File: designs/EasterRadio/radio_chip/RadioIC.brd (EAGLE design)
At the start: 38 x 29 mm, 26 parts, among them J1 S2B-NSHSS-TB, J2 S2B-NSHSS-TB, Q1 2SC3838T146, Y1 32.768kHz crystal

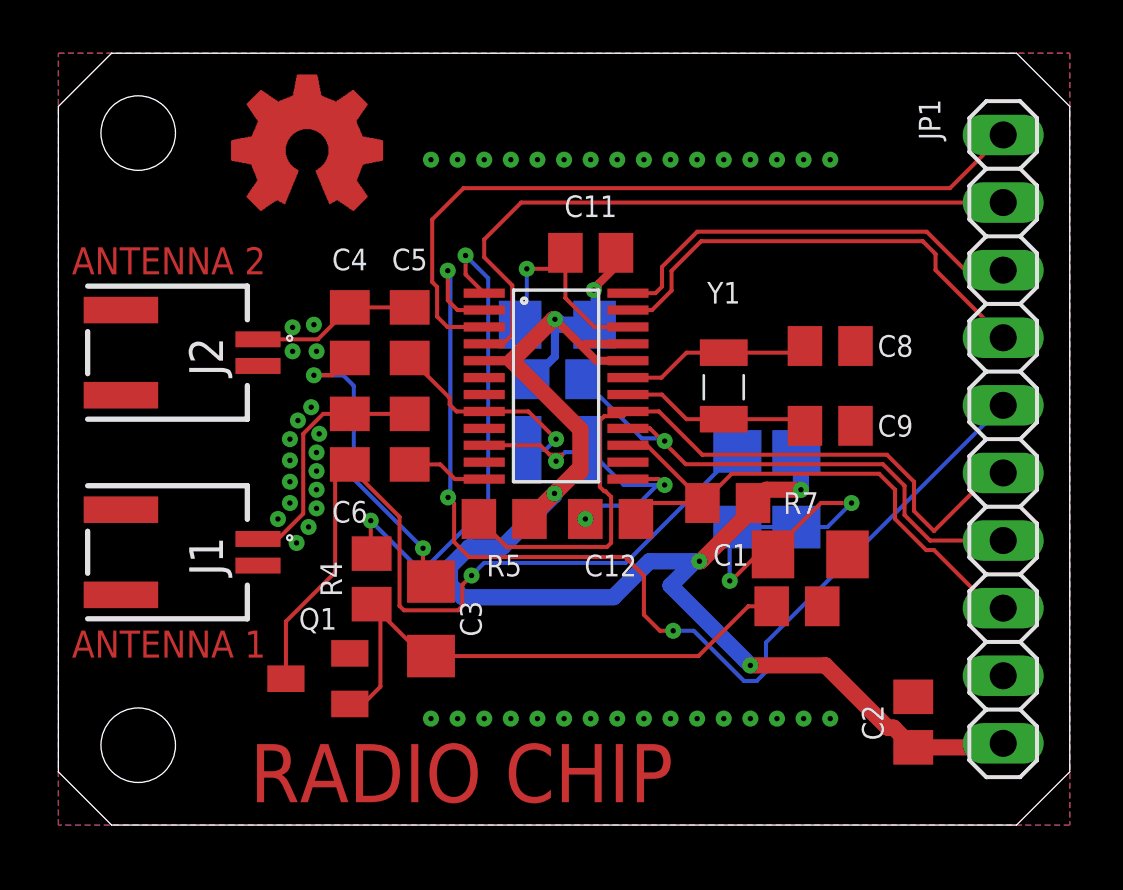
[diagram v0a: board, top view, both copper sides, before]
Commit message: added esd for rs232 to can
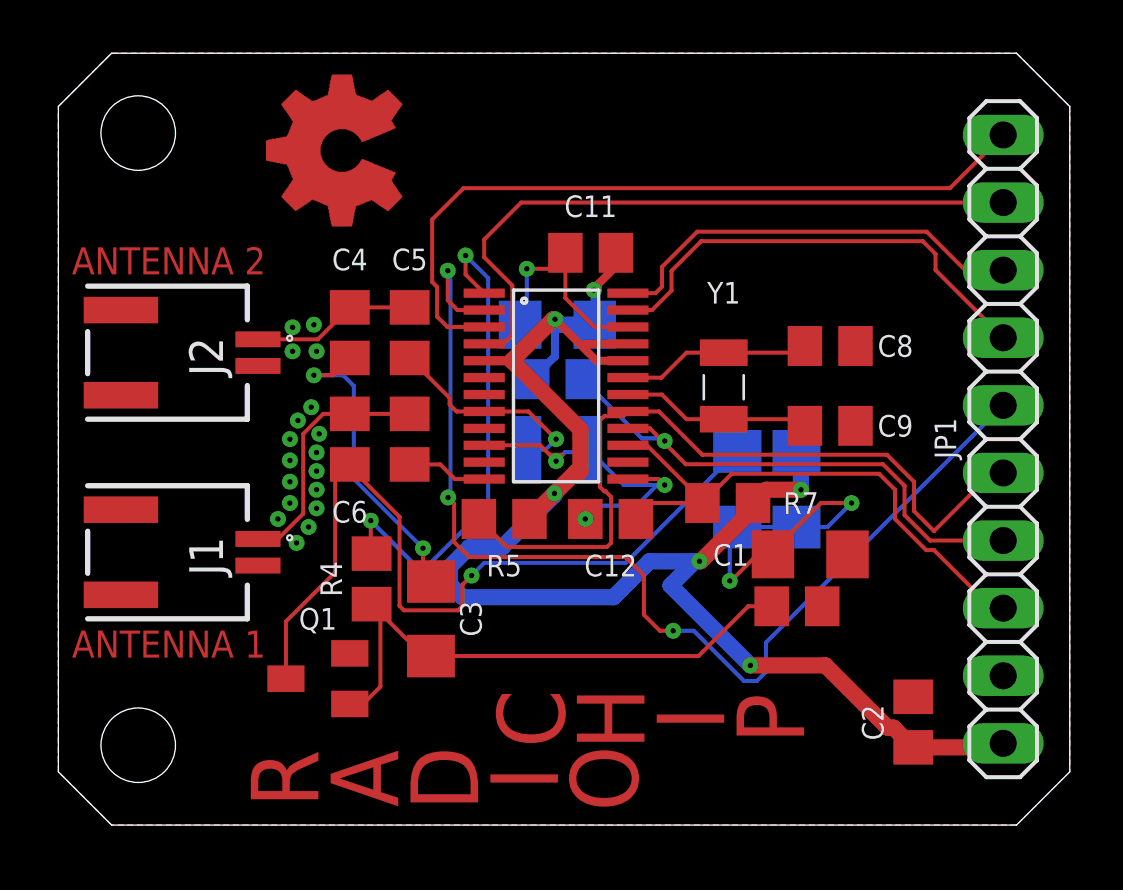
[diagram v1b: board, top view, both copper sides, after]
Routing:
- net AGND: vias 35 -> 3
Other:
- board text added: "A"
- board text added: "C"
- board text added: "D"
- board text added: "H"
- board text added: "I"
- board text added: "O"
- board text added: "P"
- board text added: "R"
- board text removed: "RADIO CHIP"

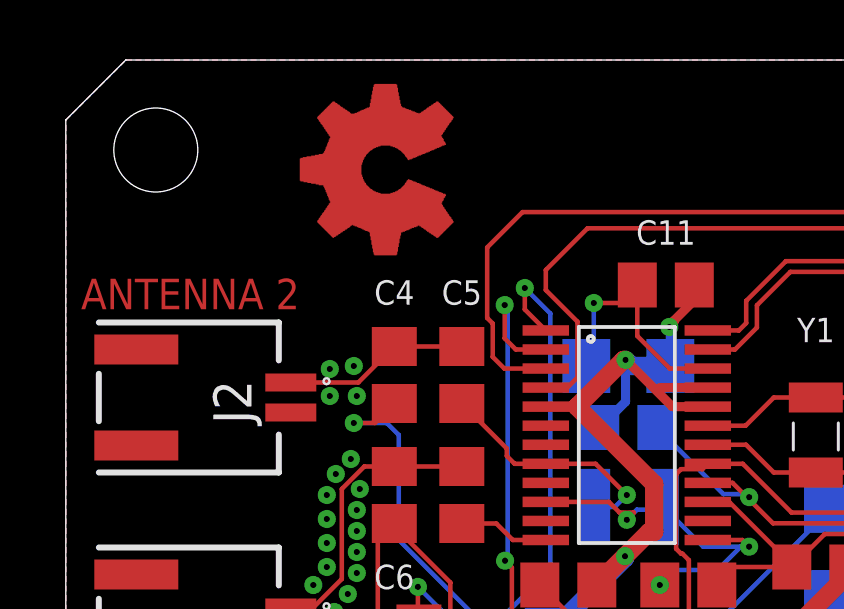
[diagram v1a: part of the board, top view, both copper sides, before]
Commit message: changes for new design excluding swap for amplifier
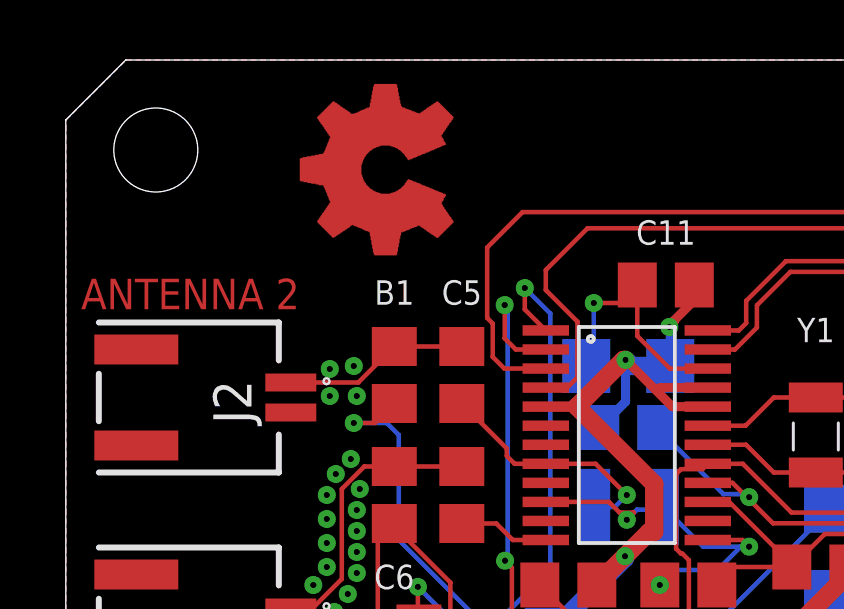
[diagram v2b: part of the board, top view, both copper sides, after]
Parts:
- B1: value 2.5K -> 2.5K Ferrit Perle
- renumbered C4 to B1
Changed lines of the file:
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@@
 <drawing>
 <settings>
-<setting alwaysvectorfont="yes"/>
+<setting alwaysvectorfont="no"/>
 <setting verticaltext="up"/>
 </settings>
@@
 </autorouter>
 <elements>
-<element name="C4" library="CommonParts" package="C0805" package3d_urn="urn:adsk.eagle:package:23617/2" value="2.5K" x="10.95" y="18.5" smashed="yes" rot="R270">
+<element name="B1" library="CommonParts" package="C0805" package3d_urn="urn:adsk.eagle:package:23617/2" value="2.5K Ferrit Perle" x="10.95" y="18.5" smashed="yes" rot="R270">
 <attribute name="NAME" x="10.95" y="21.25" size="0.8128" layer="25" rot="R180" align="center"/>
 <attribute name="POPULARITY" value="88" x="-22.07" y="-13.25" size="1.778" layer="27" rot="R270" display="off"/>
@@
 <element name="R3" library="MouserUseful" package="R1206" package3d_urn="urn:adsk.eagle:package:23540/2" value="1K" x="25.51" y="12.62" smashed="yes" rot="MR270">
 <attribute name="POPULARITY" value="41" x="58.53" y="-2.62" size="1.778" layer="28" rot="MR270" display="off"/>
-<attribute name="R3" value="" x="25.51" y="15.62" size="0.8128" layer="28" rot="MR180" align="center" display="name"/>
+<attribute name="R3" value="" x="25.51" y="15.62" size="0.8128" layer="26" rot="MR180" align="center" display="name"/>
 <attribute name="SPICEPREFIX" value="R" x="58.53" y="-2.62" size="1.778" layer="28" rot="MR270" display="off"/>
 <attribute name="WATT" value="0.5" x="58.53" y="-2.62" size="1.778" layer="28" rot="MR270" display="off"/>
@@
 <signal name="ANT2">
 <contactref element="C5" pad="2"/>
-<contactref element="C4" pad="1"/>
+<contactref element="B1" pad="1"/>
 <contactref element="J2" pad="1"/>
 <wire x1="10.95" y1="19.45" x2="9.75" y2="18.25" width="0.1524" layer="1"/>
@@
 <signal name="N$3">
 <contactref element="C3" pad="1"/>
-<contactref element="C4" pad="2"/>
+<contactref element="B1" pad="2"/>
 <wire x1="14" y1="9.15" x2="13.7" y2="9.45" width="0.1524" layer="1"/>
 <wire x1="13.7" y1="9.45" x2="13.7" y2="10.4" width="0.1524" layer="1"/>
@@
 <mfgpreviewcolor name="substratecolor" color="0xFF786E46"/>
 </mfgpreviewcolors>
+<errors>
+</errors>
 </board>
 </drawing>

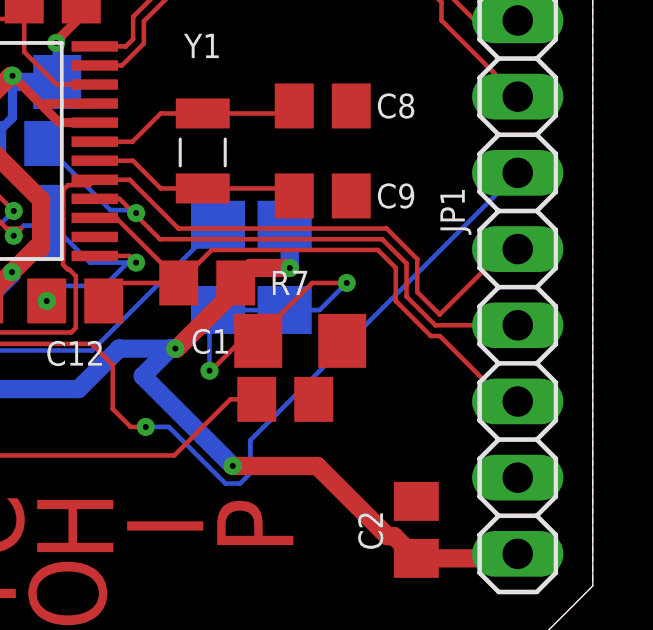
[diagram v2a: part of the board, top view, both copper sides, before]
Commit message: added changes to mainboard for speaker
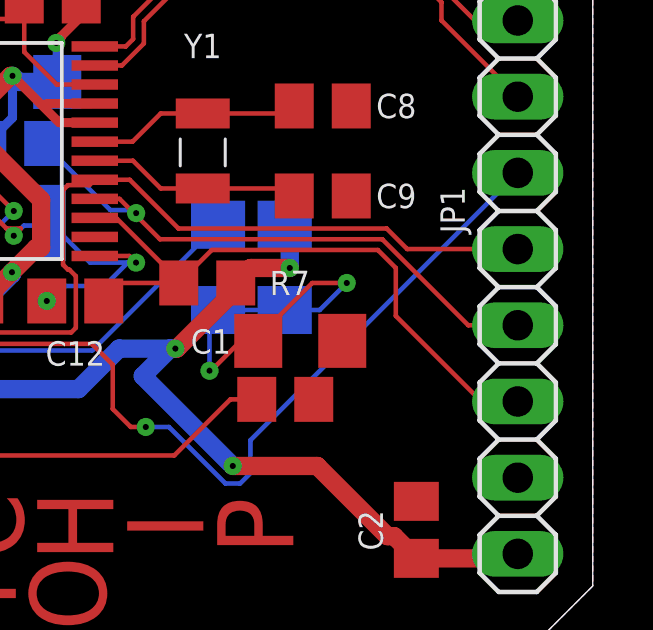
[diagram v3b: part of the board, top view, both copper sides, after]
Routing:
- net SCLK: track 29.0 -> 26.5 mm
- net SDIO: track 20.6 -> 20.0 mm
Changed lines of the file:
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@@
 <drawing>
 <settings>
-<setting alwaysvectorfont="no"/>
+<setting alwaysvectorfont="yes"/>
 <setting verticaltext="up"/>
 </settings>
@@
 </layers>
 <board>
-<fusionsync huburn="a.cGVyc29uYWw6dWUyYTNmMDU1" projecturn="a.cGVyc29uYWw6dWUyYTNmMDU1IzIwMTgxMjEwMTY0OTQ5MjI2" f3durn="urn:adsk.wipprod:dm.lineage:UHXhhLg1QYGtsfzcEnk53w" pcbguid="" lastpulledtime="" lastsyncedchangeguid="" latestrevisionid="777b2756-70f0-41dc-bc71-e2b94e35724c" lastsyncedrevisionid="777b2756-70f0-41dc-bc71-e2b94e35724c" lastboardhashguid="4fe2475e-b932-db9d-4db5-245985976be7" lastpushedtime="2020-11-29T17:03:17Z" linktopcb3d="true"/>
+<fusionsync huburn="a.cGVyc29uYWw6dWUyYTNmMDU1" projecturn="a.cGVyc29uYWw6dWUyYTNmMDU1IzIwMTgxMjEwMTY0OTQ5MjI2" f3durn="urn:adsk.wipprod:dm.lineage:_mMoevyvRculCH2RSivQfA" pcbguid="09cc48cc-a388-40bf-892d-2865ef05eea0" lastpulledtime="" lastsyncedchangeguid="" latestrevisionid="ab6607ea-bb43-46b3-8f4c-9ff7a98132cc" lastsyncedrevisionid="ab6607ea-bb43-46b3-8f4c-9ff7a98132cc" lastboardhashguid="169cb45e-4d4c-4625-844c-4060f40b92e0" lastpushedtime="2021-02-03T18:49:06Z" linktopcb3d="true"/>
 <plain>
 <wire x1="2" y1="0" x2="36" y2="0" width="0" layer="20"/>
@@
 <contactref element="SI4844-A101" pad="SDIO"/>
 <contactref element="JP1" pad="7"/>
-<wire x1="32.75195625" y1="10.69" x2="31.7926" y2="11.64935625" width="0.1524" layer="1"/>
-<wire x1="31.7926" y1="12.74804375" x2="30.98324375" y2="13.5574" width="0.1524" layer="1"/>
+<wire x1="33.85064375" y1="10.69" x2="30.98324375" y2="13.5574" width="0.1524" layer="1"/>
 <wire x1="22.224996875" y1="14.905" x2="21.4" y2="14.905" width="0.1524" layer="1"/>
 <wire x1="23.572596875" y1="13.5574" x2="22.789996875" y2="14.34" width="0.1524" layer="1"/>
 <wire x1="22.789996875" y1="14.34" x2="22.224996875" y2="14.905" width="0.1524" layer="1"/>
-<wire x1="35.5" y1="10.69" x2="32.75195625" y2="10.69" width="0.1524" layer="1"/>
-<wire x1="31.7926" y1="11.64935625" x2="31.7926" y2="12.74804375" width="0.1524" layer="1"/>
+<wire x1="35.5" y1="10.69" x2="33.85064375" y2="10.69" width="0.1524" layer="1"/>
 <wire x1="30.98324375" y1="13.5574" x2="23.572596875" y2="13.5574" width="0.1524" layer="1"/>
 <wire x1="19.7" y1="16.75" x2="21.920428125" y2="14.529571875" width="0.1524" layer="16"/>
@@
 <contactref element="SI4844-A101" pad="!RST"/>
 <contactref element="JP1" pad="8"/>
-<wire x1="35.5" y1="8.15" x2="35.0826" y2="8.15" width="0.1524" layer="1"/>
-<wire x1="35.0826" y1="8.15" x2="32.9" y2="10.3326" width="0.1524" layer="1"/>
-<wire x1="32.9" y1="10.3326" x2="32.6039125" y2="10.3326" width="0.1524" layer="1"/>
-<wire x1="32.6039125" y1="10.3326" x2="31.4352" y2="11.5013125" width="0.1524" layer="1"/>
-<wire x1="31.4352" y1="11.5013125" x2="31.4352" y2="12.6" width="0.1524" layer="1"/>
+<wire x1="35.5" y1="8.15" x2="34.2865125" y2="8.15" width="0.1524" layer="1"/>
+<wire x1="34.2865125" y1="8.15" x2="31.4352" y2="11.0013125" width="0.1524" layer="1"/>
+<wire x1="31.4352" y1="11.0013125" x2="31.4352" y2="12.6" width="0.1524" layer="1"/>
 <wire x1="31.4352" y1="12.6" x2="30.8352" y2="13.2" width="0.1524" layer="1"/>
 <wire x1="30.8352" y1="13.2" x2="25.3" y2="13.2" width="0.1524" layer="1"/>
@@
 <contactref element="SI4844-A101" pad="SCLK"/>
 <contactref element="JP1" pad="6"/>
-<wire x1="35.5" y1="13.23" x2="35.0826" y2="13.23" width="0.1524" layer="1"/>
-<wire x1="35.0826" y1="13.23" x2="32.9" y2="11.0474" width="0.1524" layer="1"/>
-<wire x1="32.9" y1="11.0474" x2="32.15" y2="11.7974" width="0.1524" layer="1"/>
-<wire x1="32.15" y1="12.8960875" x2="31.1312875" y2="13.9148" width="0.1524" layer="1"/>
+<wire x1="35.5" y1="13.23" x2="31.8160875" y2="13.23" width="0.1524" layer="1"/>
+<wire x1="31.8160875" y1="13.23" x2="31.1312875" y2="13.9148" width="0.1524" layer="1"/>
 <wire x1="22.5666625" y1="15.54" x2="21.4" y2="15.54" width="0.1524" layer="1"/>
 <wire x1="24.1918625" y1="13.9148" x2="22.5666625" y2="15.54" width="0.1524" layer="1"/>
-<wire x1="32.15" y1="11.7974" x2="32.15" y2="12.8960875" width="0.1524" layer="1"/>
 <wire x1="31.1312875" y1="13.9148" x2="24.1918625" y2="13.9148" width="0.1524" layer="1"/>
 <wire x1="20.508525" y1="12.5438" x2="20.3438" y2="12.708525" width="0.1524" layer="1"/>
@@
 </signals>
 <mfgpreviewcolors>
-<mfgpreviewcolor name="soldermaskcolor" color="0xC8008000"/>
+<mfgpreviewcolor name="soldermaskcolor" color="0xC8000000"/>
 <mfgpreviewcolor name="silkscreencolor" color="0xFFFEFEFE"/>
 <mfgpreviewcolor name="backgroundcolor" color="0xFF282828"/>

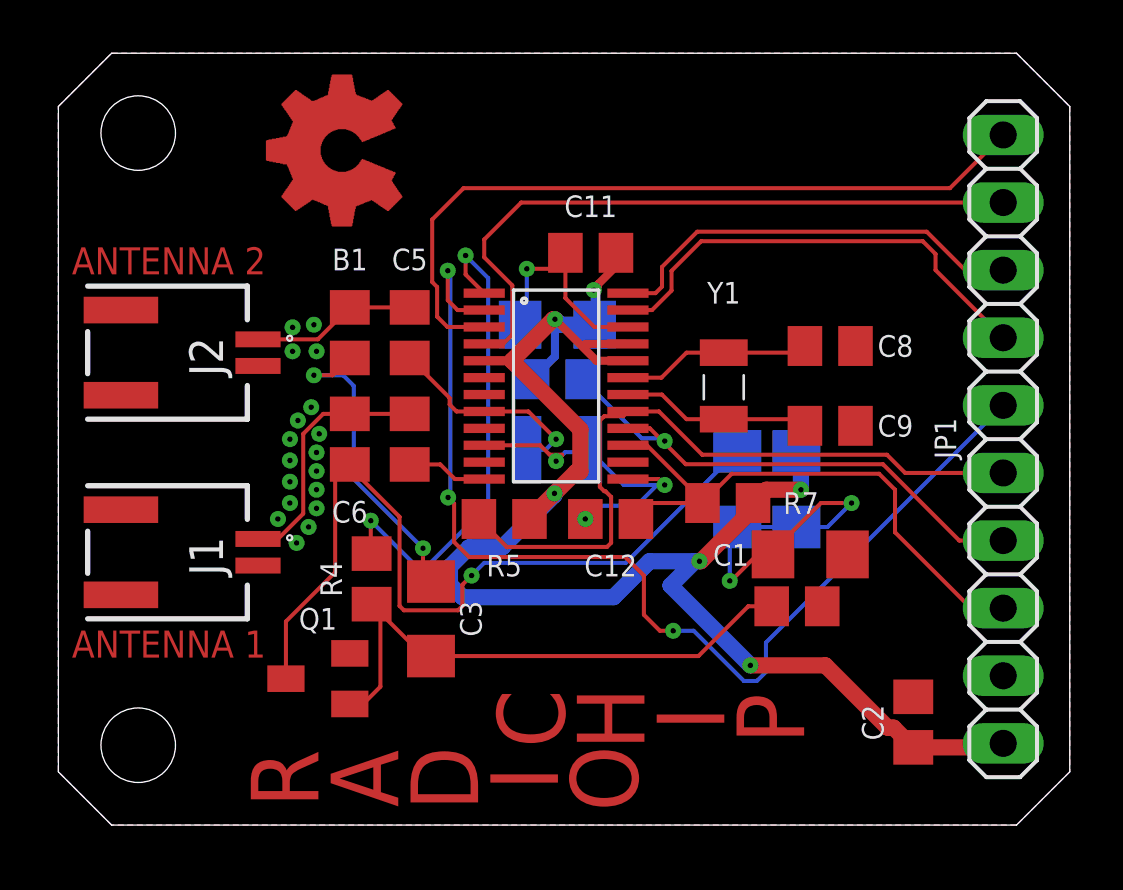
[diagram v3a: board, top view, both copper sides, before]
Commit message: added new design of radio parts added 3.3V mark
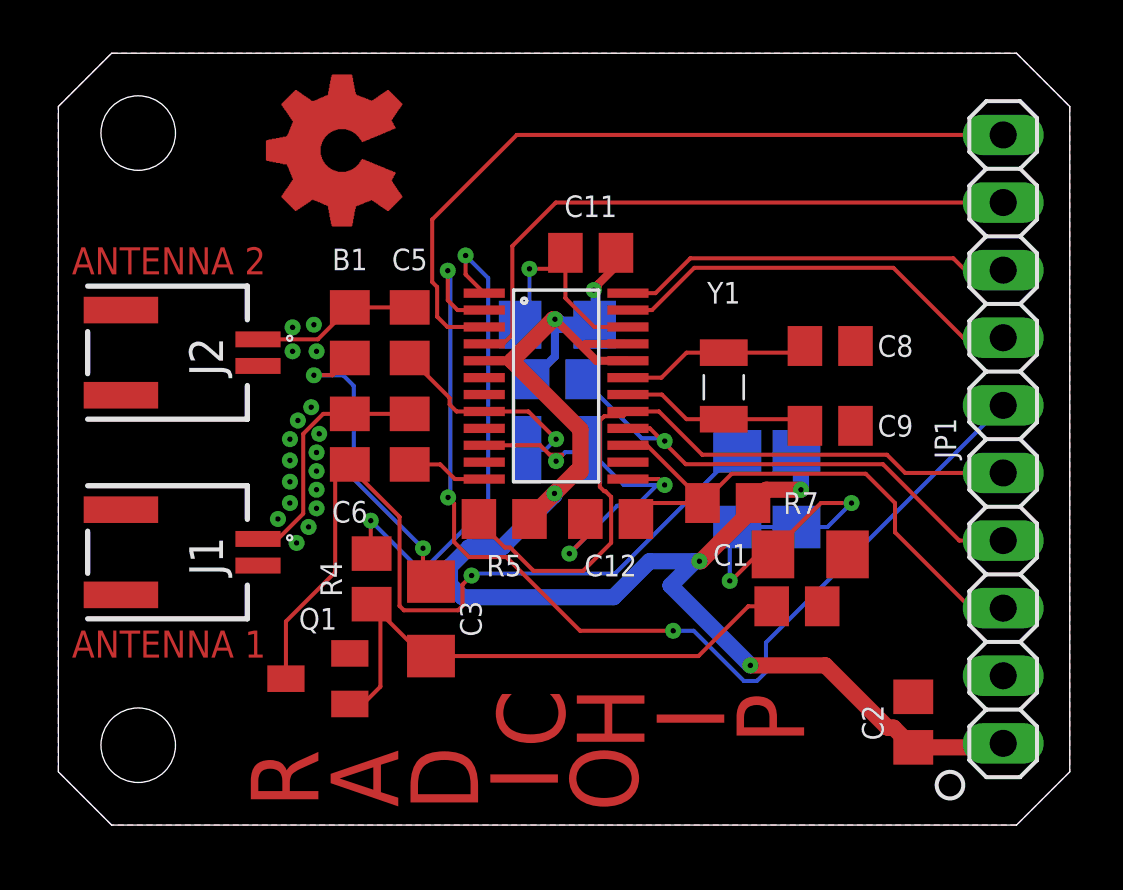
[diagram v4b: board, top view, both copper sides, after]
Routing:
- net AGND: track 13.0 -> 15.7 mm
- net TUNE2: track 25.3 -> 23.7 mm
- net ROUT: track 17.5 -> 15.8 mm
- net LOUT: track 16.1 -> 14.8 mm
- net SCLK: track 26.5 -> 27.4 mm
- net IRQ: track 41.6 -> 40.7 mm
